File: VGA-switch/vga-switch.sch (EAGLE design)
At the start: 0 parts

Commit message: a few components
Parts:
- added K1, K2, K3, K4, K5, K6, K7, K8: RR2A, relay:RR2A
- added U$1: 2.1MMJACKTHM, adafruit:2.1MMJACKTHM

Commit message: added more components
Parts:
- added LED1: (no value), led:LED5MM
- added R1: (no value), resistor:R-US_0207/10
- added S1: (no value), antitronics:ROCKERSWITCH
- added X1, X2: D-SUB15-HDR15RA, con-thomas-betts:D-SUB15-HDR15RA
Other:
- moved on the sheet: K1, K2, K3, K4, K5, K6, K7, K8, U$1
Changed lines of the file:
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@@
 <part name="K7" library="relay" deviceset="RR2A" device=""/>
 <part name="K8" library="relay" deviceset="RR2A" device=""/>
+<part name="X1" library="con-thomas-betts" deviceset="D-SUB15-" device="HDR15RA"/>
+<part name="X2" library="con-thomas-betts" deviceset="D-SUB15-" device="HDR15RA"/>
+<part name="S1" library="antitronics" deviceset="ROCKERSWITCH" device=""/>
+<part name="LED1" library="led" deviceset="LED" device="5MM"/>
+<part name="R1" library="resistor" deviceset="R-US_" device="0207/10"/>
 </parts>
 <sheets>
@@
 </plain>
 <instances>
-<instance part="U$1" gate="G$1" x="-27.94" y="10.16"/>
-<instance part="K1" gate="1" x="35.56" y="63.5" rot="R90"/>
-<instance part="K1" gate="2" x="35.56" y="78.74" rot="R90"/>
-<instance part="K1" gate="3" x="35.56" y="86.36" rot="R90"/>
-<instance part="K2" gate="1" x="58.42" y="63.5" rot="R90"/>
-<instance part="K2" gate="2" x="58.42" y="78.74" rot="R90"/>
-<instance part="K2" gate="3" x="58.42" y="86.36" rot="R90"/>
-<instance part="K3" gate="1" x="81.28" y="63.5" rot="R90"/>
-<instance part="K3" gate="2" x="81.28" y="78.74" rot="R90"/>
-<instance part="K3" gate="3" x="81.28" y="86.36" rot="R90"/>
-<instance part="K4" gate="1" x="101.6" y="63.5" rot="R90"/>
-<instance part="K4" gate="2" x="101.6" y="78.74" rot="R90"/>
-<instance part="K4" gate="3" x="101.6" y="86.36" rot="R90"/>
-<instance part="K5" gate="1" x="119.38" y="63.5" rot="R90"/>
-<instance part="K5" gate="2" x="119.38" y="78.74" rot="R90"/>
-<instance part="K5" gate="3" x="119.38" y="86.36" rot="R90"/>
-<instance part="K6" gate="1" x="137.16" y="63.5" rot="R90"/>
-<instance part="K6" gate="2" x="137.16" y="78.74" rot="R90"/>
-<instance part="K6" gate="3" x="137.16" y="86.36" rot="R90"/>
-<instance part="K7" gate="1" x="154.94" y="63.5" rot="R90"/>
-<instance part="K7" gate="2" x="154.94" y="78.74" rot="R90"/>
-<instance part="K7" gate="3" x="154.94" y="86.36" rot="R90"/>
-<instance part="K8" gate="1" x="15.24" y="63.5" rot="R90"/>
-<instance part="K8" gate="2" x="15.24" y="78.74" rot="R90"/>
-<instance part="K8" gate="3" x="15.24" y="86.36" rot="R90"/>
+<instance part="U$1" gate="G$1" x="-53.34" y="7.62"/>
+<instance part="K1" gate="1" x="12.7" y="7.62" rot="R180"/>
+<instance part="K1" gate="2" x="43.18" y="99.06" rot="R90"/>
+<instance part="K1" gate="3" x="43.18" y="104.14" rot="R90"/>
+<instance part="K2" gate="1" x="25.4" y="7.62" rot="R180"/>
+<instance part="K2" gate="2" x="43.18" y="88.9" rot="R90"/>
+<instance part="K2" gate="3" x="43.18" y="93.98" rot="R90"/>
+<instance part="K3" gate="1" x="38.1" y="7.62" rot="R180"/>
+<instance part="K3" gate="2" x="43.18" y="78.74" rot="R90"/>
+<instance part="K3" gate="3" x="43.18" y="83.82" rot="R90"/>
+<instance part="K4" gate="1" x="50.8" y="7.62" rot="R180"/>
+<instance part="K4" gate="2" x="43.18" y="68.58" rot="R90"/>
+<instance part="K4" gate="3" x="43.18" y="73.66" rot="R90"/>
+<instance part="K5" gate="1" x="63.5" y="7.62" rot="R180"/>
+<instance part="K5" gate="2" x="43.18" y="58.42" rot="R90"/>
+<instance part="K5" gate="3" x="43.18" y="63.5" rot="R90"/>
+<instance part="K6" gate="1" x="76.2" y="7.62" rot="R180"/>
+<instance part="K6" gate="2" x="43.18" y="48.26" rot="R90"/>
+<instance part="K6" gate="3" x="43.18" y="53.34" rot="R90"/>
+<instance part="K7" gate="1" x="88.9" y="7.62" rot="R180"/>
+<instance part="K7" gate="2" x="43.18" y="38.1" rot="R90"/>
+<instance part="K7" gate="3" x="43.18" y="43.18" rot="R90"/>
+<instance part="K8" gate="1" x="101.6" y="7.62" rot="R180"/>
+<instance part="K8" gate="2" x="43.18" y="27.94" rot="R90"/>
+<instance part="K8" gate="3" x="43.18" y="33.02" rot="R90"/>
+<instance part="X1" gate="-1" x="99.06" y="83.82"/>
+<instance part="X1" gate="-2" x="99.06" y="81.28"/>
+<instance part="X1" gate="-3" x="99.06" y="78.74"/>
+<instance part="X1" gate="-4" x="99.06" y="76.2"/>
+<instance part="X1" gate="-5" x="99.06" y="73.66"/>
+<instance part="X1" gate="-6" x="99.06" y="71.12"/>
+<instance part="X1" gate="-7" x="99.06" y="68.58"/>
+<instance part="X1" gate="-8" x="99.06" y="66.04"/>
+<instance part="X1" gate="-9" x="99.06" y="63.5"/>
+<instance part="X1" gate="-10" x="99.06" y="60.96"/>
+<instance part="X1" gate="-11" x="99.06" y="58.42"/>
+<instance part="X1" gate="-12" x="99.06" y="55.88"/>
+<instance part="X1" gate="-13" x="99.06" y="53.34"/>
+<instance part="X1" gate="-14" x="99.06" y="50.8"/>
+<instance part="X1" gate="-15" x="99.06" y="48.26"/>
+<instance part="X2" gate="-1" x="-12.7" y="50.8" rot="R180"/>
+<instance part="X2" gate="-2" x="-12.7" y="53.34" rot="R180"/>
+<instance part="X2" gate="-3" x="-12.7" y="55.88" rot="R180"/>
+<instance part="X2" gate="-4" x="-12.7" y="58.42" rot="R180"/>
+<instance part="X2" gate="-5" x="-12.7" y="60.96" rot="R180"/>
+<instance part="X2" gate="-6" x="-12.7" y="63.5" rot="R180"/>
+<instance part="X2" gate="-7" x="-12.7" y="66.04" rot="R180"/>
+<instance part="X2" gate="-8" x="-12.7" y="68.58" rot="R180"/>
+<instance part="X2" gate="-9" x="-12.7" y="71.12" rot="R180"/>
+<instance part="X2" gate="-10" x="-12.7" y="73.66" rot="R180"/>
+<instance part="X2" gate="-11" x="-12.7" y="76.2" rot="R180"/>
+<instance part="X2" gate="-12" x="-12.7" y="78.74" rot="R180"/>
+<instance part="X2" gate="-13" x="-12.7" y="81.28" rot="R180"/>
+<instance part="X2" gate="-14" x="-12.7" y="83.82" rot="R180"/>
+<instance part="X2" gate="-15" x="-12.7" y="86.36" rot="R180"/>
+<instance part="S1" gate="2" x="-35.56" y="12.7" rot="R270"/>
+<instance part="LED1" gate="G$1" x="127" y="12.7" rot="R90"/>
+<instance part="R1" gate="G$1" x="114.3" y="12.7"/>
 </instances>
 <busses>

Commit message: Started wiring
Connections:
- new net N$1: S1.P, U$1.TIP
- new net N$2: K11.1, K21.1, K31.1, K41.1, K51.1, K61.1, K71.1, K81.1, LED1.C, S1.B, U$1.RING
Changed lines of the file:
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@@
 </busses>
 <nets>
+<net name="N$1" class="0">
+<segment>
+<pinref part="U$1" gate="G$1" pin="TIP"/>
+<pinref part="S1" gate="2" pin="P"/>
+<wire x1="-48.26" y1="10.16" x2="-40.64" y2="10.16" width="0.1524" layer="91"/>
+</segment>
+</net>
+<net name="N$2" class="0">
+<segment>
+<pinref part="U$1" gate="G$1" pin="RING"/>
+<pinref part="S1" gate="2" pin="B"/>
+<wire x1="-48.26" y1="5.08" x2="-40.64" y2="5.08" width="0.1524" layer="91"/>
+<wire x1="-40.64" y1="5.08" x2="-40.64" y2="0" width="0.1524" layer="91"/>
+<pinref part="K1" gate="1" pin="1"/>
+<wire x1="-40.64" y1="0" x2="10.16" y2="0" width="0.1524" layer="91"/>
+<wire x1="10.16" y1="0" x2="12.7" y2="2.54" width="0.1524" layer="91"/>
+<wire x1="12.7" y1="2.54" x2="15.24" y2="0" width="0.1524" layer="91"/>
+<pinref part="K2" gate="1" pin="1"/>
+<wire x1="15.24" y1="0" x2="22.86" y2="0" width="0.1524" layer="91"/>
+<wire x1="22.86" y1="0" x2="25.4" y2="2.54" width="0.1524" layer="91"/>
+<wire x1="25.4" y1="2.54" x2="27.94" y2="0" width="0.1524" layer="91"/>
+<pinref part="K3" gate="1" pin="1"/>
+<wire x1="27.94" y1="0" x2="35.56" y2="0" width="0.1524" layer="91"/>
+<wire x1="35.56" y1="0" x2="38.1" y2="2.54" width="0.1524" layer="91"/>
+<wire x1="38.1" y1="2.54" x2="40.64" y2="0" width="0.1524" layer="91"/>
+<pinref part="K4" gate="1" pin="1"/>
+<wire x1="40.64" y1="0" x2="48.26" y2="0" width="0.1524" layer="91"/>
+<wire x1="48.26" y1="0" x2="50.8" y2="2.54" width="0.1524" layer="91"/>
+<wire x1="50.8" y1="2.54" x2="53.34" y2="0" width="0.1524" layer="91"/>
+<pinref part="K5" gate="1" pin="1"/>
+<wire x1="53.34" y1="0" x2="60.96" y2="0" width="0.1524" layer="91"/>
+<wire x1="60.96" y1="0" x2="63.5" y2="2.54" width="0.1524" layer="91"/>
+<wire x1="63.5" y1="2.54" x2="66.04" y2="0" width="0.1524" layer="91"/>
+<pinref part="K6" gate="1" pin="1"/>
+<wire x1="66.04" y1="0" x2="73.66" y2="0" width="0.1524" layer="91"/>
+<wire x1="73.66" y1="0" x2="76.2" y2="2.54" width="0.1524" layer="91"/>
+<wire x1="76.2" y1="2.54" x2="78.74" y2="0" width="0.1524" layer="91"/>
+<pinref part="K7" gate="1" pin="1"/>
+<wire x1="78.74" y1="0" x2="86.36" y2="0" width="0.1524" layer="91"/>
+<wire x1="86.36" y1="0" x2="88.9" y2="2.54" width="0.1524" layer="91"/>
+<wire x1="88.9" y1="2.54" x2="91.44" y2="0" width="0.1524" layer="91"/>
+<pinref part="K8" gate="1" pin="1"/>
+<wire x1="91.44" y1="0" x2="99.06" y2="0" width="0.1524" layer="91"/>
+<wire x1="99.06" y1="0" x2="101.6" y2="2.54" width="0.1524" layer="91"/>
+<wire x1="101.6" y1="2.54" x2="134.62" y2="2.54" width="0.1524" layer="91"/>
+<wire x1="134.62" y1="2.54" x2="134.62" y2="12.7" width="0.1524" layer="91"/>
+<pinref part="LED1" gate="G$1" pin="C"/>
+<wire x1="134.62" y1="12.7" x2="132.08" y2="12.7" width="0.1524" layer="91"/>
+</segment>
+</net>
 </nets>
 </sheet>

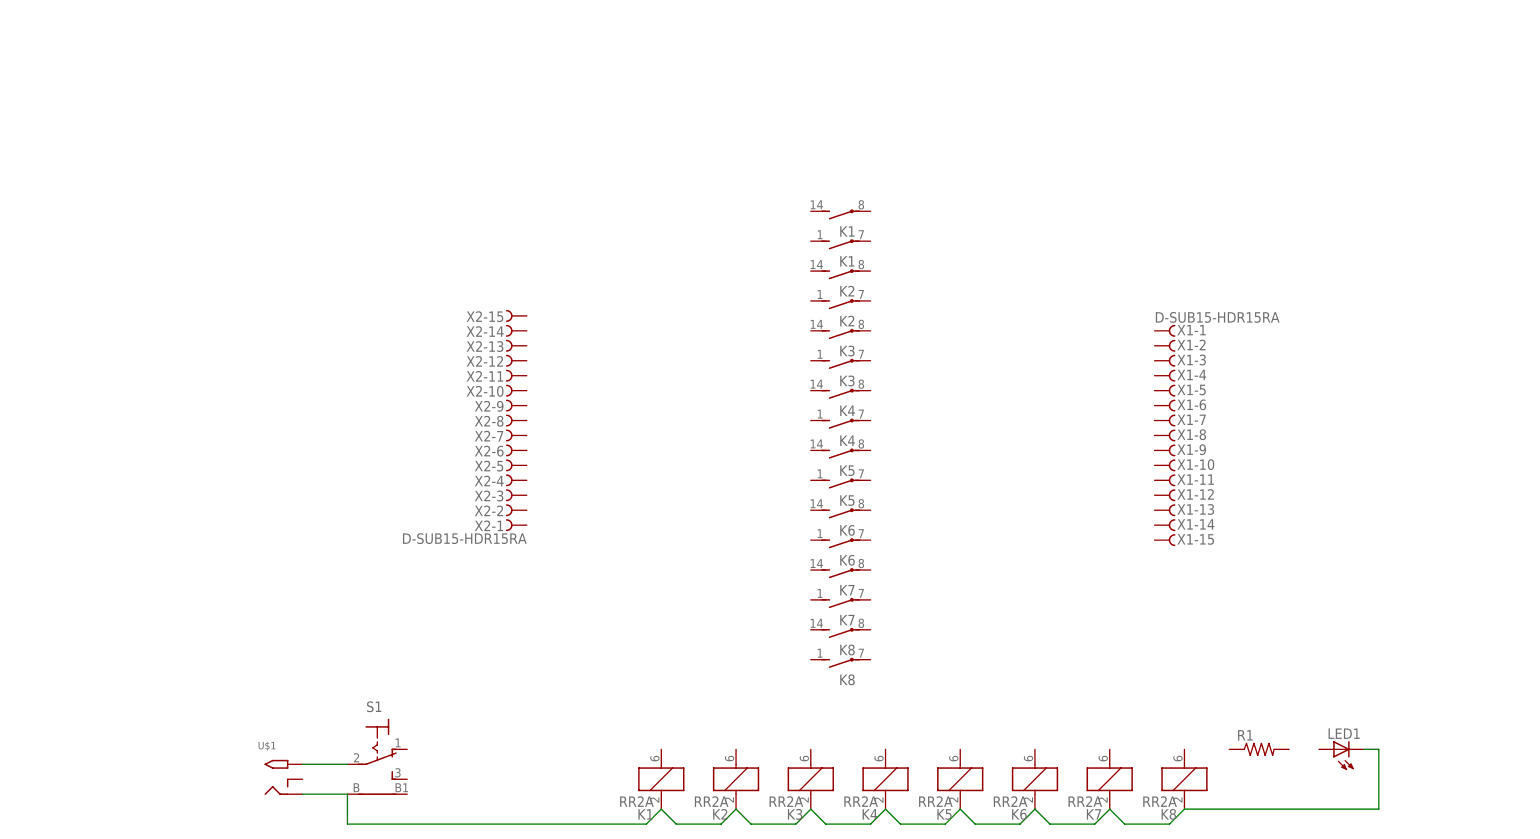
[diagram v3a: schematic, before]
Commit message: first pass at routing
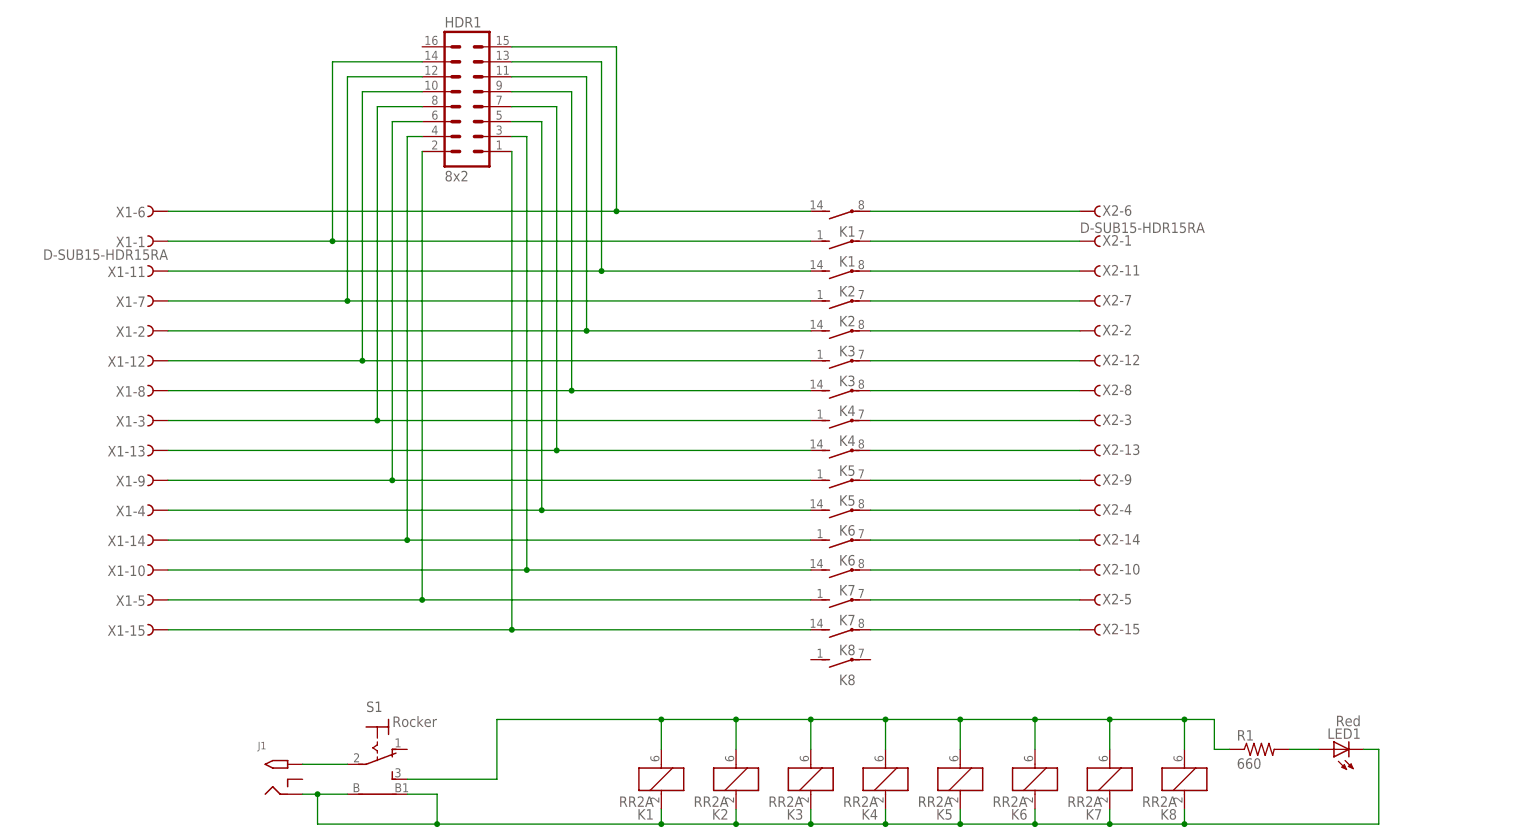
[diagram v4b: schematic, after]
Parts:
- added HDR1: 8x2, con-lstb:MA08-2
- LED1: value (none) -> Red
- R1: value (none) -> 660
- S1: value (none) -> Rocker
- renumbered U$1 to J1
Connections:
- new net N$10: HDR1.10, K32.S, X1-12.F
- new net N$11: HDR1.9, K43.S, X1-8.F
- new net N$12: HDR1.8, K42.S, X1-3.F
- new net N$13: HDR1.7, K53.S, X1-13.F
- new net N$14: HDR1.6, K52.S, X1-9.F
- new net N$15: HDR1.5, K63.S, X1-4.F
- new net N$16: HDR1.4, K62.S, X1-14.F
- new net N$17: HDR1.3, K73.S, X1-10.F
- new net N$18: HDR1.2, K72.S, X1-5.F
- new net N$19: HDR1.1, K83.S, X1-15.F
- new net N$20: K11.2, K21.2, K31.2, K41.2, K51.2, K61.2, K71.2, K81.2, R1.1, S1.S
- new net N$3: HDR1.15, K13.S, X1-6.F
- new net N$33: K13.P, X2-6.F
- new net N$34: K12.P, X2-1.F
- new net N$35: K23.P, X2-11.F
- new net N$36: K22.P, X2-7.F
- new net N$37: K33.P, X2-2.F
- new net N$38: K32.P, X2-12.F
- new net N$39: K43.P, X2-8.F
- new net N$40: K42.P, X2-3.F
- new net N$41: K53.P, X2-13.F
- new net N$42: K52.P, X2-9.F
- new net N$43: K63.P, X2-4.F
- new net N$44: K62.P, X2-14.F
- new net N$45: K73.P, X2-10.F
- new net N$46: K72.P, X2-5.F
- new net N$47: K83.P, X2-15.F
- new net N$5: LED1.A, R1.2
- new net N$6: HDR1.14, K12.S, X1-1.F
- new net N$7: HDR1.13, K23.S, X1-11.F
- new net N$8: HDR1.12, K22.S, X1-7.F
- new net N$9: HDR1.11, K33.S, X1-2.F
- net N$2: now also S1.B1
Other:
- moved on the sheet: X1-1, X1-10, X1-11, X1-12, X1-13, X1-14, X1-15, X1-2, X1-3, X1-4, X1-5, X1-6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

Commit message: board changes, layout, and logo work
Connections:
- removed net N$20: K11.2, K21.2, K31.2, K41.2, K51.2, K61.2, K71.2, K81.2, R1.1, S1.S
- new net N$4: K11.1, K21.1, K31.1, K41.1, K51.1, K61.1, K71.1, K81.1, R1.1, S1.S
- net N$2: now also K11.2, K21.2, K31.2, K41.2, K51.2, K61.2, K71.2, K81.2; no longer K11.1, K21.1, K31.1, K41.1, K51.1, K61.1, K71.1, K81.1
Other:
- moved on the sheet: K1, K2, K3, K4, K5, K6, K7, K8
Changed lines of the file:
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@@
 <instances>
 <instance part="J1" gate="G$1" x="-53.34" y="7.62"/>
-<instance part="K1" gate="1" x="12.7" y="7.62" rot="R180"/>
+<instance part="K1" gate="1" x="12.7" y="7.62"/>
 <instance part="K1" gate="2" x="43.18" y="99.06" rot="R90"/>
 <instance part="K1" gate="3" x="43.18" y="104.14" rot="R90"/>
-<instance part="K2" gate="1" x="25.4" y="7.62" rot="R180"/>
+<instance part="K2" gate="1" x="25.4" y="7.62"/>
 <instance part="K2" gate="2" x="43.18" y="88.9" rot="R90"/>
 <instance part="K2" gate="3" x="43.18" y="93.98" rot="R90"/>
-<instance part="K3" gate="1" x="38.1" y="7.62" rot="R180"/>
+<instance part="K3" gate="1" x="38.1" y="7.62"/>
 <instance part="K3" gate="2" x="43.18" y="78.74" rot="R90"/>
 <instance part="K3" gate="3" x="43.18" y="83.82" rot="R90"/>
-<instance part="K4" gate="1" x="50.8" y="7.62" rot="R180"/>
+<instance part="K4" gate="1" x="50.8" y="7.62"/>
 <instance part="K4" gate="2" x="43.18" y="68.58" rot="R90"/>
 <instance part="K4" gate="3" x="43.18" y="73.66" rot="R90"/>
-<instance part="K5" gate="1" x="63.5" y="7.62" rot="R180"/>
+<instance part="K5" gate="1" x="63.5" y="7.62"/>
 <instance part="K5" gate="2" x="43.18" y="58.42" rot="R90"/>
 <instance part="K5" gate="3" x="43.18" y="63.5" rot="R90"/>
-<instance part="K6" gate="1" x="76.2" y="7.62" rot="R180"/>
+<instance part="K6" gate="1" x="76.2" y="7.62"/>
 <instance part="K6" gate="2" x="43.18" y="48.26" rot="R90"/>
 <instance part="K6" gate="3" x="43.18" y="53.34" rot="R90"/>
-<instance part="K7" gate="1" x="88.9" y="7.62" rot="R180"/>
+<instance part="K7" gate="1" x="88.9" y="7.62"/>
 <instance part="K7" gate="2" x="43.18" y="38.1" rot="R90"/>
 <instance part="K7" gate="3" x="43.18" y="43.18" rot="R90"/>
-<instance part="K8" gate="1" x="101.6" y="7.62" rot="R180"/>
+<instance part="K8" gate="1" x="101.6" y="7.62"/>
 <instance part="K8" gate="2" x="43.18" y="27.94" rot="R90"/>
 <instance part="K8" gate="3" x="43.18" y="33.02" rot="R90"/>
@@
 <junction x="-45.72" y="5.08"/>
 <junction x="-25.4" y="0"/>
-<pinref part="K1" gate="1" pin="1"/>
+<pinref part="K1" gate="1" pin="2"/>
 <wire x1="12.7" y1="2.54" x2="12.7" y2="0" width="0.1524" layer="91"/>
-<pinref part="K2" gate="1" pin="1"/>
+<pinref part="K2" gate="1" pin="2"/>
 <wire x1="25.4" y1="2.54" x2="25.4" y2="0" width="0.1524" layer="91"/>
-<pinref part="K3" gate="1" pin="1"/>
+<pinref part="K3" gate="1" pin="2"/>
 <wire x1="38.1" y1="2.54" x2="38.1" y2="0" width="0.1524" layer="91"/>
-<pinref part="K4" gate="1" pin="1"/>
+<pinref part="K4" gate="1" pin="2"/>
 <wire x1="50.8" y1="2.54" x2="50.8" y2="0" width="0.1524" layer="91"/>
-<pinref part="K5" gate="1" pin="1"/>
+<pinref part="K5" gate="1" pin="2"/>
 <wire x1="63.5" y1="2.54" x2="63.5" y2="0" width="0.1524" layer="91"/>
-<pinref part="K6" gate="1" pin="1"/>
+<pinref part="K6" gate="1" pin="2"/>
 <wire x1="76.2" y1="2.54" x2="76.2" y2="0" width="0.1524" layer="91"/>
-<pinref part="K7" gate="1" pin="1"/>
+<pinref part="K7" gate="1" pin="2"/>
 <wire x1="88.9" y1="2.54" x2="88.9" y2="0" width="0.1524" layer="91"/>
-<pinref part="K8" gate="1" pin="1"/>
+<pinref part="K8" gate="1" pin="2"/>
 <wire x1="101.6" y1="2.54" x2="101.6" y2="0" width="0.1524" layer="91"/>
 <junction x="12.7" y="0"/>
@@
 </segment>
 </net>
-<net name="N$20" class="0">
+<net name="N$4" class="0">
 <segment>
 <pinref part="S1" gate="2" pin="S"/>
 <wire x1="-30.48" y1="7.62" x2="-15.24" y2="7.62" width="0.1524" layer="91"/>
 <wire x1="-15.24" y1="7.62" x2="-15.24" y2="17.78" width="0.1524" layer="91"/>
+<pinref part="R1" gate="G$1" pin="1"/>
+<wire x1="106.68" y1="12.7" x2="109.22" y2="12.7" width="0.1524" layer="91"/>
+<wire x1="106.68" y1="17.78" x2="106.68" y2="12.7" width="0.1524" layer="91"/>
 <wire x1="-15.24" y1="17.78" x2="12.7" y2="17.78" width="0.1524" layer="91"/>
+<pinref part="K1" gate="1" pin="1"/>
 <wire x1="12.7" y1="17.78" x2="25.4" y2="17.78" width="0.1524" layer="91"/>
 <wire x1="25.4" y1="17.78" x2="38.1" y2="17.78" width="0.1524" layer="91"/>
@@
 <wire x1="88.9" y1="17.78" x2="101.6" y2="17.78" width="0.1524" layer="91"/>
 <wire x1="101.6" y1="17.78" x2="106.68" y2="17.78" width="0.1524" layer="91"/>
-<wire x1="106.68" y1="17.78" x2="106.68" y2="12.7" width="0.1524" layer="91"/>
-<pinref part="R1" gate="G$1" pin="1"/>
-<wire x1="106.68" y1="12.7" x2="109.22" y2="12.7" width="0.1524" layer="91"/>
-<pinref part="K1" gate="1" pin="2"/>
 <wire x1="12.7" y1="12.7" x2="12.7" y2="17.78" width="0.1524" layer="91"/>
-<pinref part="K2" gate="1" pin="2"/>
+<pinref part="K2" gate="1" pin="1"/>
 <wire x1="25.4" y1="12.7" x2="25.4" y2="17.78" width="0.1524" layer="91"/>
-<pinref part="K3" gate="1" pin="2"/>
+<pinref part="K3" gate="1" pin="1"/>
 <wire x1="38.1" y1="12.7" x2="38.1" y2="17.78" width="0.1524" layer="91"/>
-<pinref part="K4" gate="1" pin="2"/>
+<pinref part="K4" gate="1" pin="1"/>
 <wire x1="50.8" y1="12.7" x2="50.8" y2="17.78" width="0.1524" layer="91"/>
+<pinref part="K5" gate="1" pin="1"/>
+<wire x1="63.5" y1="12.7" x2="63.5" y2="17.78" width="0.1524" layer="91"/>
+<pinref part="K6" gate="1" pin="1"/>
+<wire x1="76.2" y1="12.7" x2="76.2" y2="17.78" width="0.1524" layer="91"/>
+<pinref part="K7" gate="1" pin="1"/>
+<wire x1="88.9" y1="12.7" x2="88.9" y2="17.78" width="0.1524" layer="91"/>
+<pinref part="K8" gate="1" pin="1"/>
+<wire x1="101.6" y1="12.7" x2="101.6" y2="17.78" width="0.1524" layer="91"/>
 <junction x="12.7" y="17.78"/>
 <junction x="25.4" y="17.78"/>
 <junction x="38.1" y="17.78"/>
 <junction x="50.8" y="17.78"/>
-<pinref part="K5" gate="1" pin="2"/>
-<wire x1="63.5" y1="12.7" x2="63.5" y2="17.78" width="0.1524" layer="91"/>
-<pinref part="K6" gate="1" pin="2"/>
-<wire x1="76.2" y1="12.7" x2="76.2" y2="17.78" width="0.1524" layer="91"/>
-<pinref part="K7" gate="1" pin="2"/>
-<wire x1="88.9" y1="12.7" x2="88.9" y2="17.78" width="0.1524" layer="91"/>
-<pinref part="K8" gate="1" pin="2"/>
-<wire x1="101.6" y1="12.7" x2="101.6" y2="17.78" width="0.1524" layer="91"/>
 <junction x="63.5" y="17.78"/>
 <junction x="76.2" y="17.78"/>
